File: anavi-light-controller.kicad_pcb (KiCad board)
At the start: 2 copper layers, 80 x 40.6 mm, 22 parts, among them J1 Screw_Terminal_1x04, P1 CONN_01X03, Q1 IRF8721PBF-1, Q2 IRF8721PBF-1, Q3 IRF8721PBF-1, SW1 SW_DIP_x01, U1 I2C_SENS_1, U2 I2C_SENS_1, U3 I2C_SENS_1

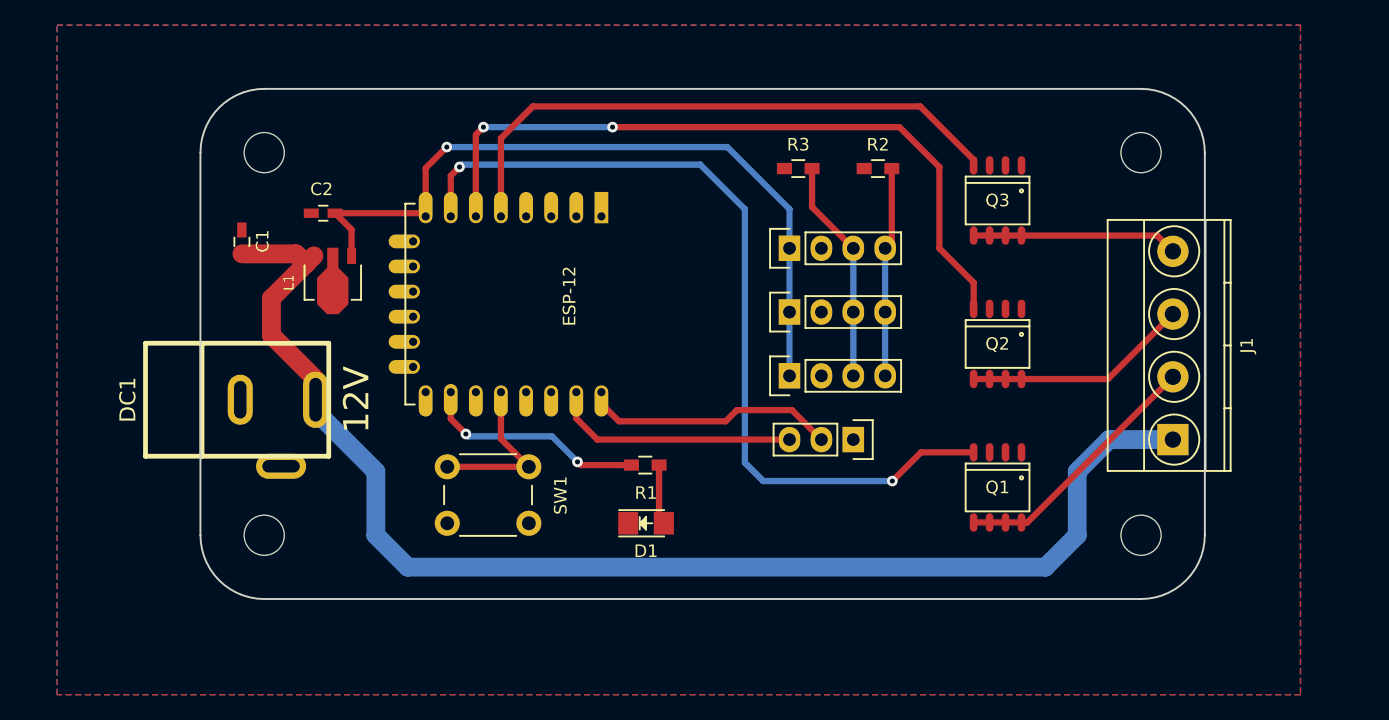
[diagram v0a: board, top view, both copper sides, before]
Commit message: anavi-light-controller: Add labels
Signed-off-by: Leon Anavi <leon@anavi.org>
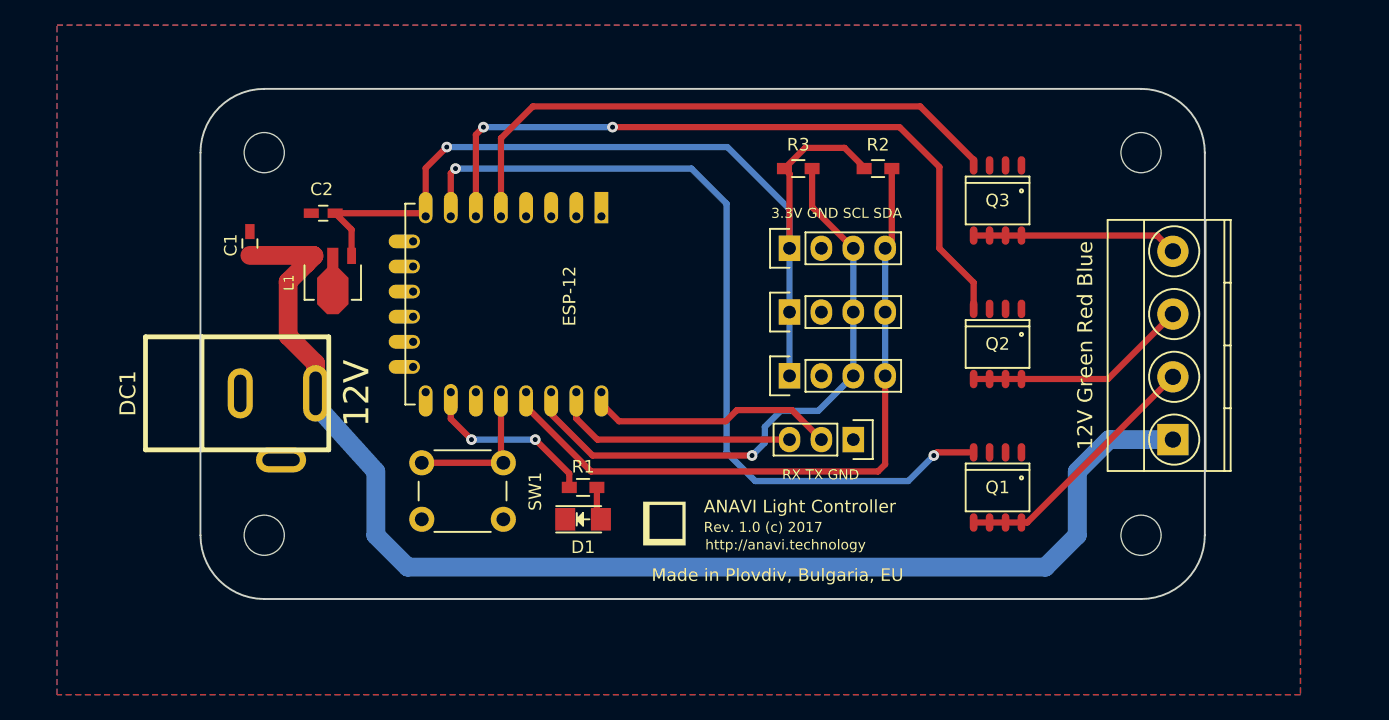
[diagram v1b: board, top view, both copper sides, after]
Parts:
- added G***: LOGO, logo:anavi-logo, F.Cu at (101.7, 105.8)
- moved R1 5.26 mm to (95.2, 102.9)
- moved D1 5.03 mm to (95.2, 105.4)
- moved SW1 2.06 mm to (88.9, 105.4)
- moved C1 0.65 mm to (68.7, 83.4)
- moved DC1 0.51 mm to (67.7, 95.4)
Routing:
- net Net-(ESP-12-Pad13): track 17.0 -> 56.2 mm
- net Net-(ESP-12-Pad14): track 17.9 -> 48.4 mm, vias 0 -> 1
- net +3V3: track 60.1 -> 74.4 mm
- net Net-(ESP-12-Pad10): track 18.0 -> 14.5 mm
- net Net-(D1-Pad2): track 4.79 -> 2.67 mm
- net Net-(ESP-12-Pad12): track 13.4 -> 12.2 mm
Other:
- board text added: "12V Green Red Blue"
- board text added: "3.3V GND SCL SDA"
- board text added: "ANAVI Light Controller"
- board text added: "Made in Plovdiv, Bulgaria, EU"
- board text added: "RX TX GND"
- board text added: "Rev. 1.0 (c) 2017"
- board text added: "http://anavi.technology"

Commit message: anavi-light-controller.kicad_pcb: Rotate I2C
Signed-off-by: Leon Anavi <leon@anavi.org>
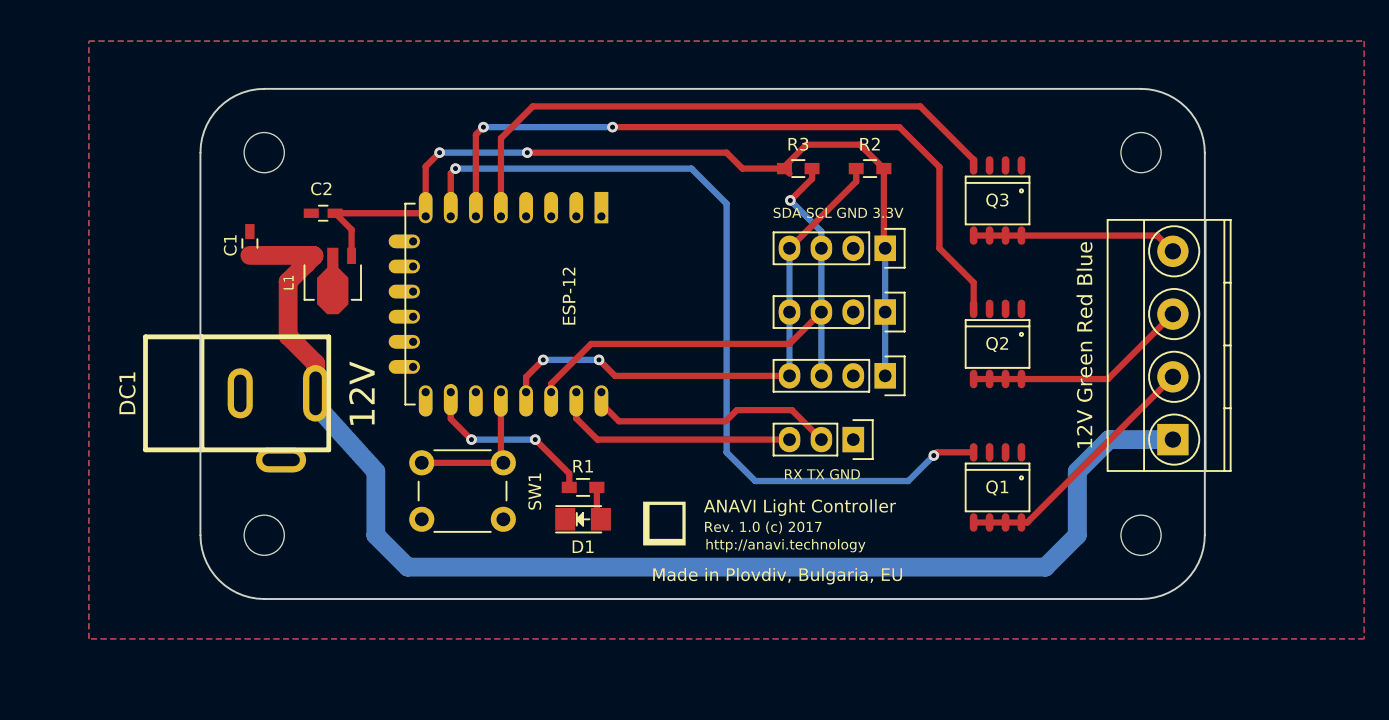
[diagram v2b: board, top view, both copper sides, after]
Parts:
- moved U1 12.7 mm to (119.3, 94.0), turned to 270 degrees
- moved U3 12.7 mm to (119.3, 83.8), turned to 270 degrees
- moved U2 7.62 mm to (119.3, 88.9), turned to 270 degrees
- moved R2 0.64 mm to (118.1, 77.5), turned to 180 degrees
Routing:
- net Net-(ESP-12-Pad13): track 56.2 -> 43.4 mm, vias 0 -> 2
- net Net-(ESP-12-Pad14): track 48.4 -> 44.6 mm
- net +3V3: track 74.4 -> 71.5 mm, vias 1 -> 2
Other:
- board text added: "SDA SCL GND 3.3V"
- board text removed: "3.3V GND SCL SDA"

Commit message: anavi-light-controller.kicad_pcb: Increase tracks
Increace 12V tracks and change the positions of
the capacitors.

Signed-off-by: Leon Anavi <leon@anavi.org>
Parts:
- moved C1 8.08 mm to (74.4, 89.2), turned to 180 degrees
- moved C2 3.69 mm to (76.2, 77.7), turned to 0 degrees
- moved L1 2.10 mm to (75.2, 84.3), turned to 90 degrees
- moved R1 1.02 mm to (95.2, 101.9)
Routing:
- net +3V3: track 71.5 -> 81.2 mm
- net +12V: track 104.3 -> 98.9 mm
- net Net-(J1-Pad2): track 20.7 -> 23.6 mm
- net Net-(D1-Pad2): track 2.67 -> 4.14 mm
- net Net-(ESP-12-Pad10): track 14.5 -> 13.2 mm
- net Net-(J1-Pad3): track 18.0 -> 19.1 mm
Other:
- net class 12V added: clearance 0.254, trace_width 1.5, via_dia 0.85, via_drill 0.4

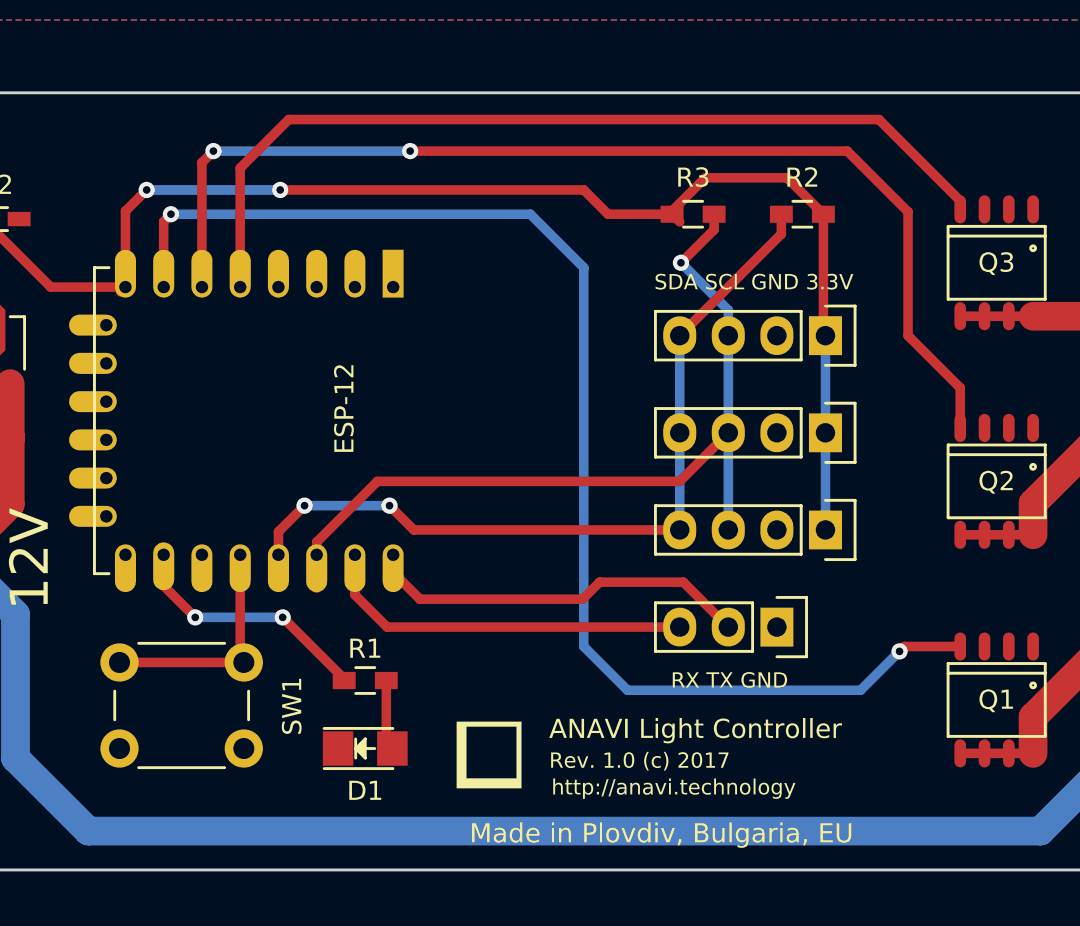
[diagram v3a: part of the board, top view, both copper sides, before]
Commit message: anavi-light-controller.kicad_pcb: no vias
Signed-off-by: Leon Anavi <leon@anavi.org>
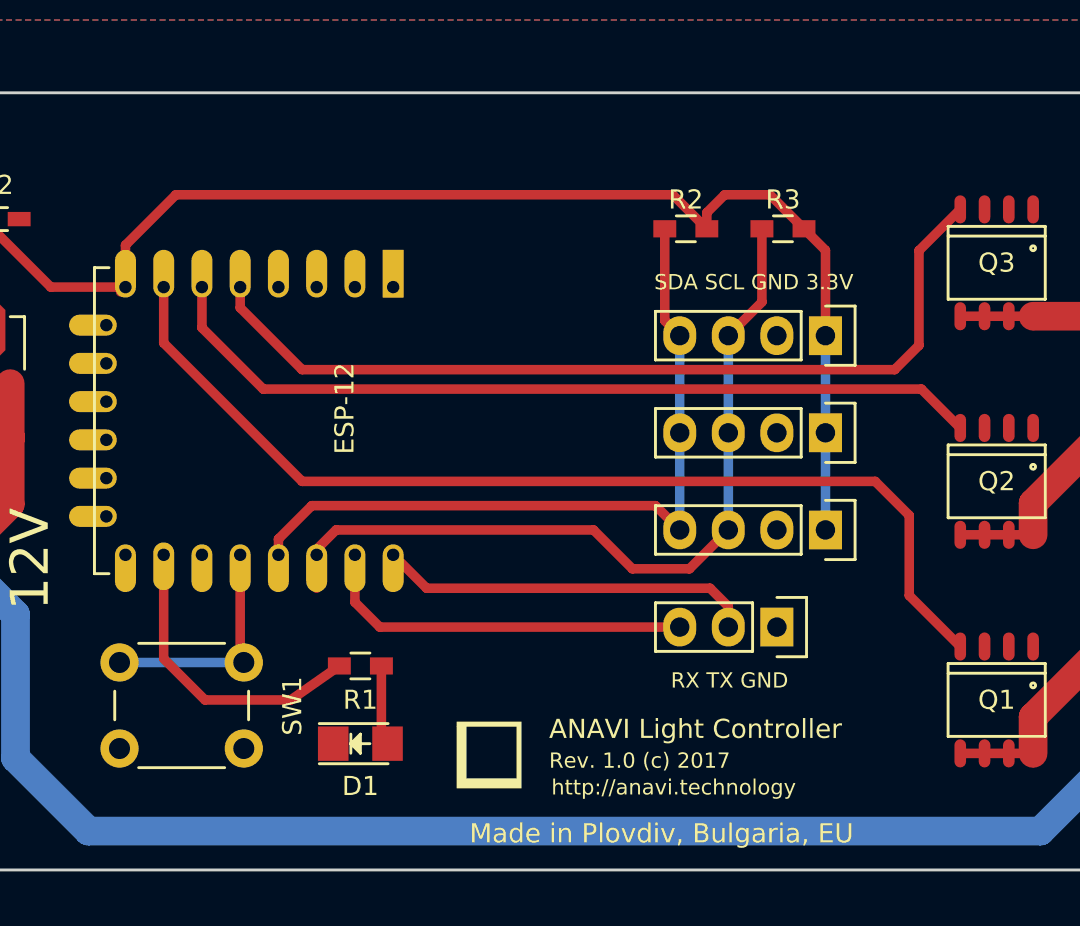
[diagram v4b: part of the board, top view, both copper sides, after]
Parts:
- moved R2 6.14 mm to (112.0, 78.2)
- moved R3 4.76 mm to (117.1, 78.2), turned to 180 degrees
- moved R1 0.80 mm to (95.0, 101.1)
- moved D1 0.36 mm to (95.0, 105.2)
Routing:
- net Net-(ESP-12-Pad7): track 68.1 -> 53.6 mm, vias 2 -> 0
- net Net-(ESP-12-Pad6): track 57.4 -> 44.0 mm, vias 2 -> 0
- net Net-(ESP-12-Pad10): track 13.2 -> 19.3 mm, vias 2 -> 0
- net Net-(ESP-12-Pad13): track 43.4 -> 40.6 mm, vias 2 -> 0
- net Net-(ESP-12-Pad14): track 44.6 -> 42.1 mm, vias 1 -> 0
- net +3V3: track 81.2 -> 78.8 mm, vias 2 -> 0

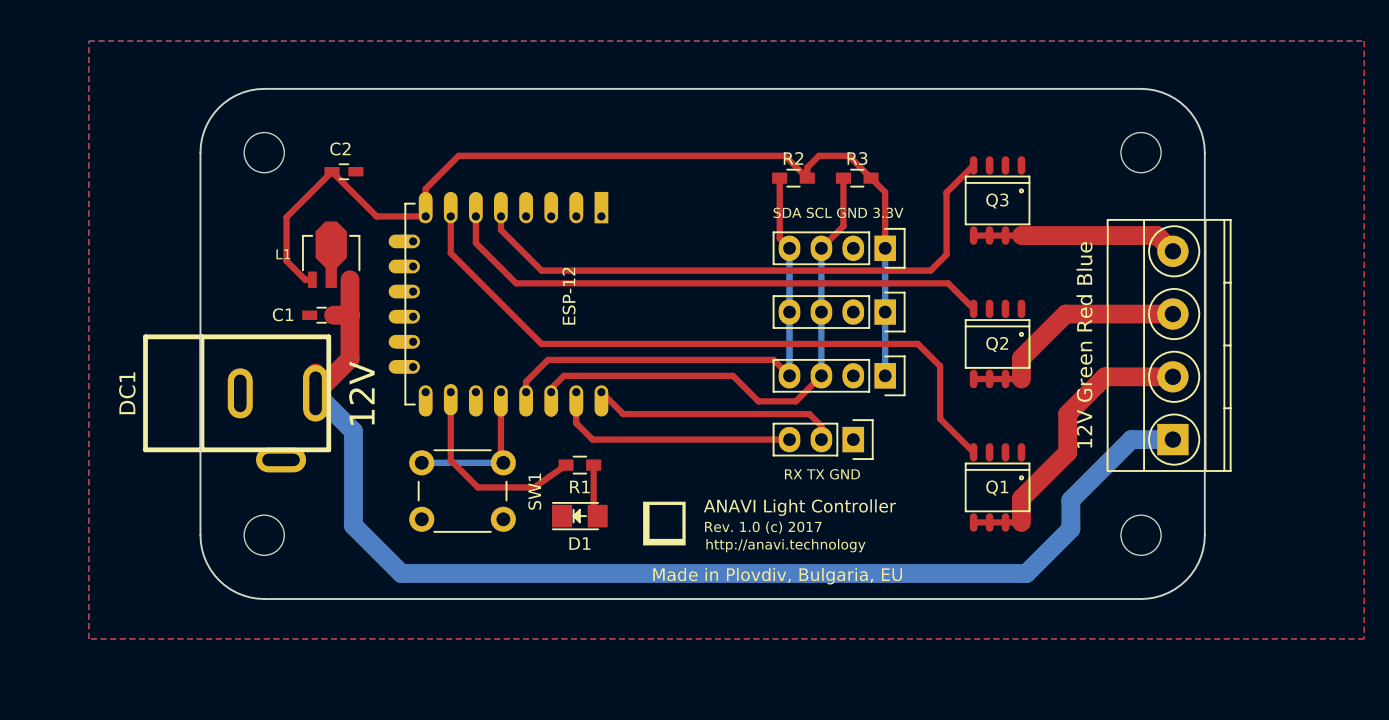
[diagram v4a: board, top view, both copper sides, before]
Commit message: anavi-light-controller.kicad_pcb: reduce
Reduce width of the PCB and change the mounting holes.

Signed-off-by: Leon Anavi <leon@anavi.org>
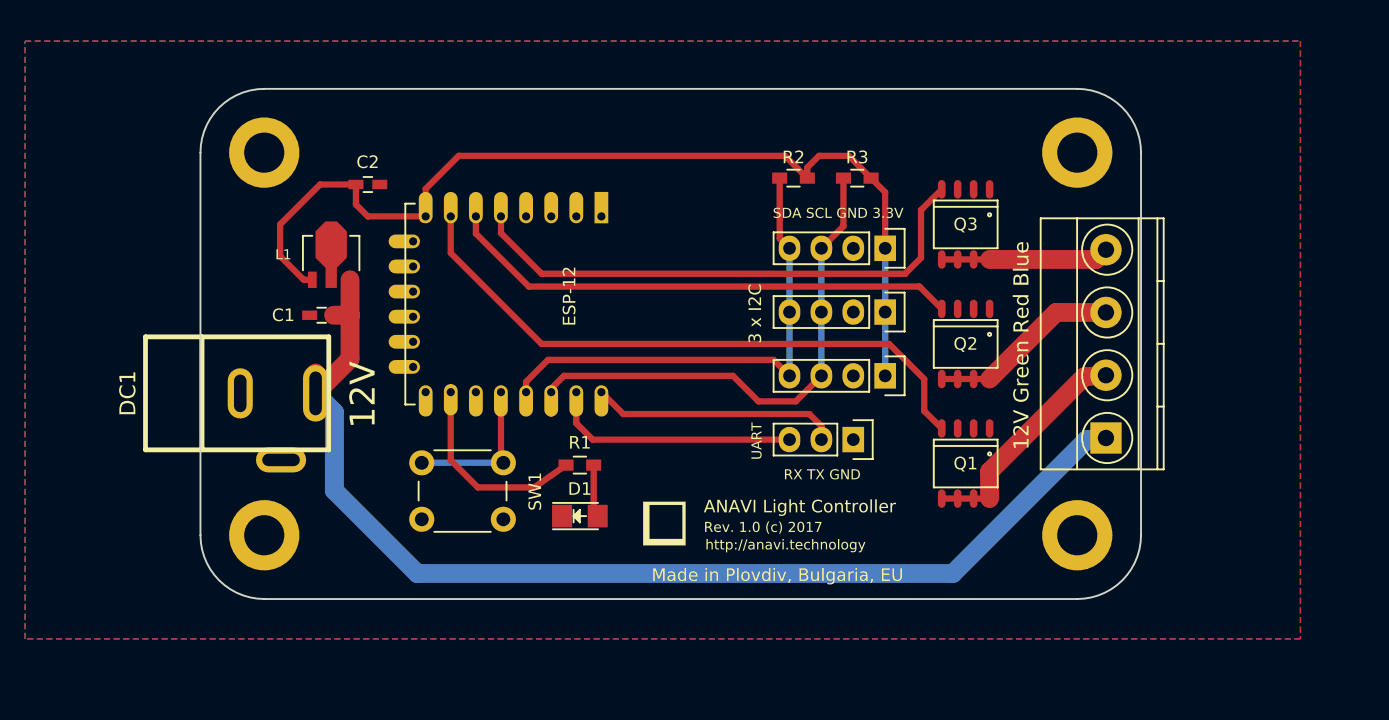
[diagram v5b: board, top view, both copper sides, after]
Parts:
- removed the REF** at (69.8, 76.2)
- removed the REF** at (69.8, 106.7)
- removed the REF** at (139.7, 106.7)
- removed the REF** at (139.7, 76.2)
- added REF**: MountingHole_3.2mm_M3_DIN965_Pad, Mounting_Holes:MountingHole_3.2mm_M3_DIN965_Pad, F.Cu at (69.8, 106.7)
- added REF**: MountingHole_3.2mm_M3_DIN965_Pad, Mounting_Holes:MountingHole_3.2mm_M3_DIN965_Pad, F.Cu at (134.6, 76.2)
- added REF**: MountingHole_3.2mm_M3_DIN965_Pad, Mounting_Holes:MountingHole_3.2mm_M3_DIN965_Pad, F.Cu at (69.8, 76.2)
- added REF**: MountingHole_3.2mm_M3_DIN965_Pad, Mounting_Holes:MountingHole_3.2mm_M3_DIN965_Pad, F.Cu at (134.6, 106.7)
- moved J1 5.34 mm to (136.9, 98.9)
- moved Q1 3.18 mm to (125.7, 101.0)
- moved Q3 3.18 mm to (125.7, 81.9)
- moved Q2 2.54 mm to (125.7, 91.4)
- moved C2 2.16 mm to (78.1, 78.7)
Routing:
- net +12V: track 98.9 -> 91.6 mm
- net Net-(J1-Pad2): track 23.6 -> 18.4 mm
- net Net-(ESP-12-Pad7): track 53.6 -> 49.3 mm
- net Net-(J1-Pad3): track 19.1 -> 15.4 mm
- net Net-(ESP-12-Pad5): track 46.9 -> 43.3 mm
- net Net-(J1-Pad4): track 16.4 -> 13.4 mm
- net Net-(ESP-12-Pad6): track 44.0 -> 41.1 mm
- net +3V3: track 78.8 -> 79.3 mm
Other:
- board size 80 x 40.6 mm -> 74.9 x 40.6 mm
- board text added: "3 x I2C"
- board text added: "UART"
